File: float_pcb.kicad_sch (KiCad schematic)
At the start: 46 parts, among them J1 BR Switch, J2 5V, J3 USB_C, J4 Conn_01x02, J5 BR_DEPTH_SENSOR, J6 BR Light, J7 Batt, Q1 AO3400A, SW2 SW_Push, SW3 ENABLE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

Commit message: First Version
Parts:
- removed J4: Conn_01x02, Connector_PinHeader_2.54mm:PinHeader_1x02_P2.54mm_Vertical, symbol Connector_Generic:Conn_01x02
- removed R18, R19: R, Resistor_SMD:R_0805_2012Metric, symbol Device:R
- removed VR1, VR2: TPSM863252RDXR, TPSM863252RDXR:VREG_TPSM863252RDXR, symbol TPSM863252RDXR:TPSM863252RDXR
- added C13: 100n, Capacitor_SMD:C_0805_2012Metric, symbol Device:C
- added C14: 1u, Capacitor_SMD:C_0805_2012Metric, symbol Device:C
- added H1, H2, H3, H4: MH, MountingHole:MountingHole_2.2mm_M2, symbol Mechanical:MountingHole
- added J8: Conn_01x04, Connector_PinHeader_2.54mm:PinHeader_1x04_P2.54mm_Vertical, symbol Connector_Generic:Conn_01x04
- added U1, U2: TPSM863252, float_pcb_footprints:TPSM86325x_RDX0007A, symbol float_pcb_symbols:TPSM86325X
- C1, C6: value 10uF -> 10u
- C10, C5: value 33uF -> 33u
- C12: value 1uF -> 1u
- C2, C7: value 100nF -> 100n
- C3, C8: value 10nF -> 10n
- C4, C9: value 22pF -> 22p
- D3: value LED -> 5V_STAT
- ENABLE1: renamed from SW3; value ENABLE -> SW_Push
- J1, J2, J6: footprint Connector_JST:JST_VH_B2P-VH_1x02_P3.96mm_Vertical -> Connector_JST:JST_XH_B2B-XH-A_1x02_P2.50mm_Vertical
- J3: footprint Connector_USB:USB_C_Receptacle_HRO_TYPE-C-31-M-12 -> Connector_USB:USB_C_Receptacle_GCT_USB4105-xx-A_16P_TopMnt_Horizontal
- J5: value BR_DEPTH_SENSOR -> BR_DEPTH
- R1, R13: value 4.7kQ -> 4k7
- R10, R11: value 5.1kQ -> 5k1
- R12, R17, R3, R7: value 10kQ -> 10k
- R14: value 2.7kQ -> 2k7
- R15: value 650Q -> 650
- R16: value 1.5kQ -> 1k5; footprint LED_SMD:LED_0805_2012Metric -> Resistor_SMD:R_0805_2012Metric
- R2, R6: value 28.7kQ -> 28k7
- R4: value 135kQ -> 135k
- R5, R9: value 30kQ -> 30k
- R8: value 220kQ -> 220k
- renumbered SW2 to BOOT1
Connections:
- net +3V3: now also C13.1, C14.1, U1.3 (VOUT)
- net +BATT: now also U1.1 (VIN), U2.1 (VIN)
- net GND: now also BOOT1.2, C12.2, R11.1, C13.2, C14.2, U1.4 (PGND), U2.4 (PGND); no longer BOOT1.1, C12.1, R11.2
- net LIGHT: now also U3.22 (IO18); no longer U3.37 (IO41)
- net at C10.1, C9.1, J2.1 (Pin_1)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: now also U2.3 (VOUT)
- net at C9.2, R8.2, R9.1: now also U2.7 (FB)
- net at R6.2, R7.1: now also C8.1, U2.6 (EN)
- net at J3.B5 (CC2): now also R11.2; no longer R11.1
- net at ENABLE1.1, R12.2, U3.45 (EN): now also C12.1; no longer C12.2
- net at C4.2, R4.2, R5.1: now also U1.7 (FB)
- net at U3.4 (IO0): now also BOOT1.1; no longer BOOT1.2
- net USB_VBUS_UNUSED: now reaches J3.A4 (VBUS), J3.A9 (VBUS), J3.B4 (VBUS), J3.B9 (VBUS)
- net at C3.1: now also R2.2, R3.1, U1.6 (EN)
- net at U3.35 (IO39): now also J8.1 (Pin_1)
- net at U3.36 (IO40): now also J8.2 (Pin_2)
- net at U3.38 (IO42): now also J8.4 (Pin_4)
- new net: J8.3 (Pin_3), U3.37 (IO41)
- no-connect marks 38 -> 33
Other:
- note added: "3V3 Buck Convertor"
- note added: "5V Buck Convertor"
- note added: "Battery Input"
- note added: "Blue Robotics Light Setup"
- note added: "ESP32 Setup"
- note added: "Mounting Holes"
- company: (none) -> Leviathan Underwater Robotics (Evan Kim)
- title: (none) -> Float PCB
- moved on the sheet: BOOT1, C1, C10, C12, C2, C3, C4, C5, C6, C7, C8, C9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

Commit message: V2
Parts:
- removed H3, H4: MH, MountingHole:MountingHole_2.2mm_M2, symbol Mechanical:MountingHole
- removed J2: 5V, Connector_JST:JST_XH_B2B-XH-A_1x02_P2.50mm_Vertical, symbol Connector_Generic:Conn_01x02
- removed J8: Conn_01x04, Connector_PinHeader_2.54mm:PinHeader_1x04_P2.54mm_Vertical, symbol Connector_Generic:Conn_01x04
- removed U3: ESP32-S3-MINI-1U, RF_Module:ESP32-S2-MINI-1U, symbol RF_Module:ESP32-S3-MINI-1U
- added J4: Conn_01x03, Connector_JST:JST_XH_B3B-XH-A_1x03_P2.50mm_Vertical, symbol Connector_Generic:Conn_01x03
- added J9: I2C, Connector_JST:JST_XH_B4B-XH-A_1x04_P2.50mm_Vertical, symbol Connector_Generic:Conn_01x04
- added LS1: SMT-0540-T-9-R, buzzer:XDCR_SMT-0540-T-9-R, symbol Buzzer:SMT-0540-T-9-R
- added Q2: AO3400A, Package_TO_SOT_SMD:SOT-23, symbol Transistor_FET:AO3400A
- added R18, R19: 4k7, Resistor_SMD:R_0603_1608Metric, symbol Device:R
- added R20: 10k, Resistor_SMD:R_0603_1608Metric, symbol Device:R
- added U4: ESP32-S3-WROOM-1, RF_Module:ESP32-S3-WROOM-1U, symbol RF_Module:ESP32-S3-WROOM-1
- C1, C10, C12, C13, C14, C2, C3, C4, C5, C6, C7, C8, C9: footprint Capacitor_SMD:C_0805_2012Metric -> Capacitor_SMD:C_0603_1608Metric
- D1: value BATT_STAT -> BATT; footprint LED_SMD:LED_0805_2012Metric -> LED_SMD:LED_0603_1608Metric
- D2: value LED -> 3V3; footprint LED_SMD:LED_0805_2012Metric -> LED_SMD:LED_0603_1608Metric
- D3: value 5V_STAT -> 5V; footprint LED_SMD:LED_0805_2012Metric -> LED_SMD:LED_0603_1608Metric
- J1: value BR Switch -> Switch
- J5: value BR_DEPTH -> I2C; footprint Connector_JST:JST_GH_BM04B-GHS-TBT_1x04-1MP_P1.25mm_Vertical -> Connector_JST:JST_XH_B4B-XH-A_1x04_P2.50mm_Vertical
- J6: value BR Light -> Light
- R1, R10, R11, R12, R13, R14, R15, R16, R17, R2, R3, R4, R5, R6, R7, R8, R9: footprint Resistor_SMD:R_0805_2012Metric -> Resistor_SMD:R_0603_1608Metric
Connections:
- net +3V3: now also J6.2 (Pin_2), J9.4 (Pin_4), LS1.LOAD+, R18.2, R19.1, U4.2 (3V3); no longer J6.1 (Pin_1)
- net +BATT: now also C1.2, C7.2, J1.1 (Pin_1); no longer C1.1, C7.1, J1.2 (Pin_2)
- net GND: now also C1.1, C7.1, J4.1 (Pin_1), J9.1 (Pin_1), Q2.2 (S), R20.1, U4.1 (GND), U4.40 (GND), U4.41 (GND); no longer C1.2, C7.2
- net LIGHT: now also U4.15 (IO3)
- net at C10.1, C9.1, R16.1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: now also J4.2 (Pin_2)
- net at C12.1, ENABLE1.1, R12.2: now also U4.3 (EN)
- net at J7.2 (Pin_2): now also J1.2 (Pin_2); no longer J1.1 (Pin_1)
- net at BOOT1.1: now also U4.27 (IO0)
- net at J3.A6 (D+), J3.B6 (D+): now also U4.14 (USB_D+)
- net at J3.A7 (D-), J3.B7 (D-): now also U4.13 (USB_D-)
- net at Q1.3 (D): now also J6.1 (Pin_1); no longer J6.2 (Pin_2)
- net SCL renamed SCL1
- net SCL1: now also U4.9 (IO16)
- net SDA renamed SDA1
- net SDA1: now also U4.10 (IO17)
- new net: LS1.LOAD-, Q2.3 (D)
- new net BUZZER: Q2.1 (G), R20.2, U4.5 (IO5)
- new net SCL2: J9.3 (Pin_3), R19.2, U4.11 (IO18)
- new net SDA2: J9.2 (Pin_2), R18.1, U4.12 (IO8)
- new net SERVO: J4.3 (Pin_3), U4.16 (IO46)
- no-connect marks 33 -> 30
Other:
- note added: "Blue Robotics Light"
- note added: "Buzzer"
- note added: "I2Cs"
- note removed: "Blue Robotics Light Setup"
- title: Float PCB -> Dory
- moved on the sheet: BOOT1, C1, C13, C7, H1, H2, J1, J6, Q1, R17

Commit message: V3
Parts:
- removed LS1: SMT-0540-T-9-R, buzzer:XDCR_SMT-0540-T-9-R, symbol Buzzer:SMT-0540-T-9-R
- added H3: MH, MountingHole:MountingHole_2.2mm_M2, symbol Mechanical:MountingHole
- added J2: Conn_01x04, Connector_PinHeader_2.54mm:PinHeader_1x04_P2.54mm_Vertical, symbol Connector_Generic:Conn_01x04
- added LS1: AT-1127-ST-2-R, buzzer:XDCR_AT-1127-ST-2-R, symbol Buzzer:AT-1127-ST-2-R
- C14: value 1u -> 22u
- R14: value 2k7 -> 4k7
- R15: value 650 -> 1k
- R16: value 1k5 -> 2k2
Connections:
- net +3V3: now also C4.2, C5.2, R15.2, R4.2, LS1.P; no longer C4.1, C5.1, R15.1, R4.1
- net +BATT: now also R14.1; no longer R14.2
- net BUZZER: now also R20.1, U4.26 (IO45); no longer R20.2, U4.5 (IO5)
- net GND: now also C10.1, C12.1, C5.1, ENABLE1.1, R11.2, R17.2, R20.2, R5.1, R9.1; no longer C10.2, C12.2, C5.2, ENABLE1.2, R11.1, R17.1, R20.1, R5.2, R9.2
- net LIGHT: now also R17.1; no longer R17.2
- net SCL1: now also U4.16 (IO46); no longer U4.9 (IO16)
- net SCL2: now also U4.24 (IO47); no longer U4.11 (IO18)
- net SDA1: now also U4.17 (IO9); no longer U4.10 (IO17)
- net SDA2: now also U4.25 (IO48); no longer U4.12 (IO8)
- net SERVO: now also U4.35 (IO42); no longer U4.16 (IO46)
- net at J4.2 (Pin_2), R16.1, U2.3 (VOUT): now also C10.2, C9.2, R8.2; no longer C10.1, C9.1, R8.1
- net at J3.B5 (CC2): now also R11.1; no longer R11.2
- net at Q2.3 (D): now also LS1.N
- net at R12.2, U4.3 (EN): now also C12.2, ENABLE1.2; no longer C12.1, ENABLE1.1
- net at U4.31 (IO38): now also J2.1 (Pin_1)
- net at U4.32 (IO39): now also J2.2 (Pin_2)
- net at U4.33 (IO40): now also J2.3 (Pin_3)
- net at U4.34 (IO41): now also J2.4 (Pin_4)
- net at D2.2 (A): now also R15.1; no longer R15.2
- net at D1.2 (A): now also R14.2; no longer R14.1
- new net: C9.1, R8.1, R9.2, U2.7 (FB)
- new net: C4.1, R4.1, R5.2, U1.7 (FB)
- no-connect marks 30 -> 26
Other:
- company: Leviathan Underwater Robotics (Evan Kim) -> Leviathan Underwater Robotics
- moved on the sheet: C10, C12, C4, C5, C9, ENABLE1, R11, R14, R15, R17, R20, R4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

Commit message: Version 3
Before the big 4 layer migration
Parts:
- added TP1: 5V, TestPoint:TestPoint_Pad_D1.5mm, symbol Connector:TestPoint
- added TP2: 3V3, TestPoint:TestPoint_Pad_D1.5mm, symbol Connector:TestPoint
- added TP3: GND, TestPoint:TestPoint_Pad_D1.5mm, symbol Connector:TestPoint
- added TP4: BATT, TestPoint:TestPoint_Pad_D1.5mm, symbol Connector:TestPoint
- added U3: USBLC6-2SC6, Package_TO_SOT_SMD:SOT-23-6, symbol Power_Protection:USBLC6-2SC6
- C1, C10, C5, C6: footprint Capacitor_SMD:C_0603_1608Metric -> Capacitor_SMD:C_0805_2012Metric
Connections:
- net +3V3: now also C4.1, TP2.1; no longer C4.2
- net +BATT: now also C1.1, C2.2, TP4.1; no longer C1.2, C2.1
- net BUZZER: now also U4.25 (IO48); no longer U4.26 (IO45)
- net GND: now also C1.2, C2.1, C3.1, ENABLE1.2, R10.2, TP3.1, U3.2 (GND); no longer C1.1, C2.2, C3.2, ENABLE1.1, R10.1
- net LIGHT: now also U4.17 (IO9); no longer U4.15 (IO3)
- net SCL1: now also U4.18 (IO10); no longer U4.16 (IO46)
- net SCL2: now also U4.23 (IO21); no longer U4.24 (IO47)
- net SDA1: now also U4.19 (IO11); no longer U4.17 (IO9)
- net SDA2: now also U4.24 (IO47); no longer U4.25 (IO48)
- net at R8.1, R9.2, U2.7 (FB): now also C9.2; no longer C9.1
- net at C10.2, J4.2 (Pin_2), R16.1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: now also C9.1, TP1.1; no longer C9.2
- net at R2.2, R3.1, U1.6 (EN): now also C3.2; no longer C3.1
- net at R4.1, R5.2, U1.7 (FB): now also C4.2; no longer C4.1
- net at C12.2, R12.2, U4.3 (EN): now also ENABLE1.1; no longer ENABLE1.2
- net at J3.A5 (CC1): now also R10.1; no longer R10.2
- net at J3.A6 (D+), J3.B6 (D+): now also U3.6 (I/O1); no longer U4.14 (USB_D+)
- net at J3.A7 (D-), J3.B7 (D-): now also U3.4 (I/O2); no longer U4.13 (USB_D-)
- net USB_VBUS_UNUSED renamed VBUS
- net VBUS: now also U3.5 (VBUS)
- new net: U3.3 (I/O2), U4.13 (USB_D-)
- new net: U3.1 (I/O1), U4.14 (USB_D+)
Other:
- company: Leviathan Underwater Robotics -> Leviathan Underwater Robotics (Evan Kim)
- moved on the sheet: C1, C10, C2, C3, C4, C5, C9, D1, D2, D3, ENABLE1, H1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

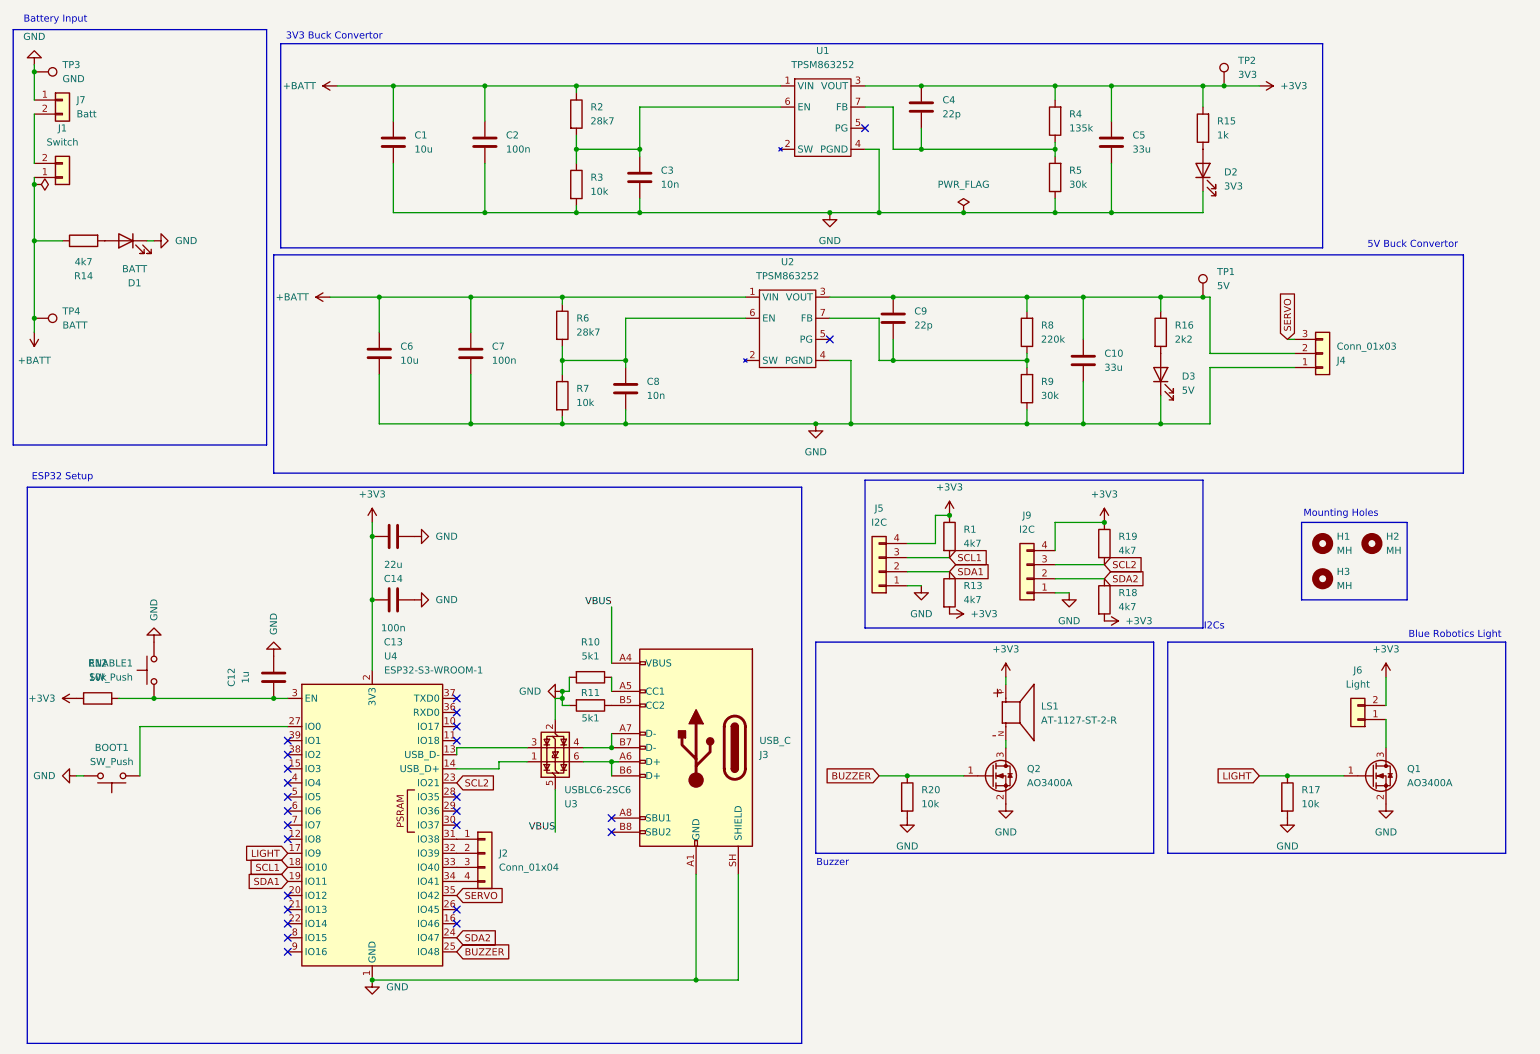
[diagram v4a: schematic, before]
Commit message: Start of the great multilayer migration
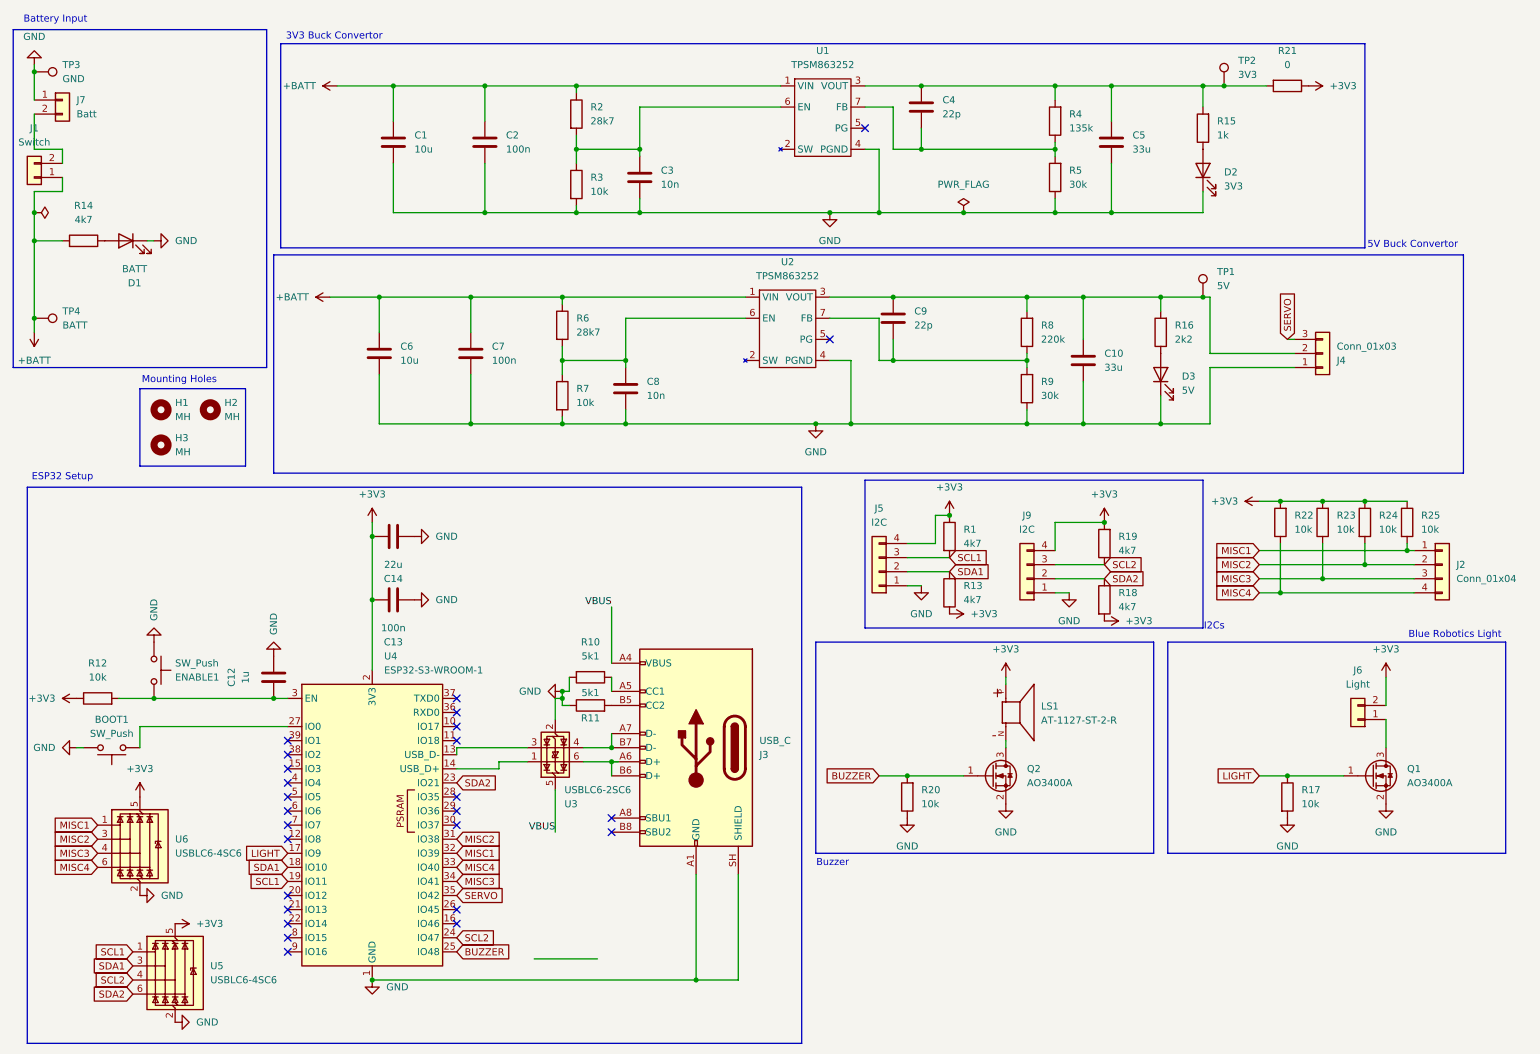
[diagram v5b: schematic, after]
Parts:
- added R21: 0, Resistor_SMD:R_0603_1608Metric, symbol Device:R
- added R22, R23, R24, R25: 10k, Resistor_SMD:R_0603_1608Metric, symbol Device:R
- added U5, U6: USBLC6-4SC6, Package_TO_SOT_SMD:SOT-23-6, symbol Power_Protection:USBLC6-4SC6
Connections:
- net +3V3: now also R13.1, R19.2, R21.1, R22.2, R23.2, R24.1, R25.1, U5.5 (VBUS), U6.5 (VBUS); no longer C4.1, C5.2, R13.2, R15.2, R19.1, R4.2, TP2.1, U1.3 (VOUT)
- net +BATT: now also R14.2; no longer R14.1
- net BUZZER: now also R20.2; no longer R20.1
- net GND: now also ENABLE1.1, R11.1, R20.1, U5.2 (GND), U6.2 (GND); no longer ENABLE1.2, R11.2, R20.2
- net SCL1: now also U4.19 (IO11), U5.1 (I/O1); no longer U4.18 (IO10)
- net SCL2: now also R19.1, U4.24 (IO47), U5.4 (I/O3); no longer R19.2, U4.23 (IO21)
- net SDA1: now also R13.2, U4.18 (IO10), U5.3 (I/O2); no longer R13.1, U4.19 (IO11)
- net SDA2: now also U4.23 (IO21), U5.6 (I/O4); no longer U4.24 (IO47)
- net at C10.2, C9.1, J4.2 (Pin_2)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: now also R16.2; no longer R16.1
- net at J3.B5 (CC2): now also R11.2; no longer R11.1
- net at C12.2, R12.2, U4.3 (EN): now also ENABLE1.2; no longer ENABLE1.1
- net at D3.2 (A): now also R16.1; no longer R16.2
- net MISC1: now reaches J2.1 (Pin_1)
- net MISC1: now also U4.32 (IO39), R25.2, U6.1 (I/O1); no longer U4.31 (IO38)
- net MISC2: now reaches J2.2 (Pin_2)
- net MISC2: now also U4.31 (IO38), R24.2, U6.3 (I/O2); no longer U4.32 (IO39)
- net MISC3: now reaches J2.3 (Pin_3)
- net MISC3: now also U4.34 (IO41), R23.1, U6.4 (I/O3); no longer U4.33 (IO40)
- net MISC4: now reaches J2.4 (Pin_4)
- net MISC4: now also U4.33 (IO40), R22.1, U6.6 (I/O4); no longer U4.34 (IO41)
- net at D1.2 (A): now also R14.1; no longer R14.2
- new net: C4.1, C5.2, R15.2, R21.2, R4.2, TP2.1, U1.3 (VOUT)
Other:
- moved on the sheet: BOOT1, ENABLE1, J1, R11, R13, R14, R16, R19, R20
